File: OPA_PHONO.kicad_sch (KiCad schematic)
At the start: 5 parts, among them J1 PJRAS2X1S01X, J2 PJRAS2X1S01X, J3 UJC-HP-3-SMT-TR

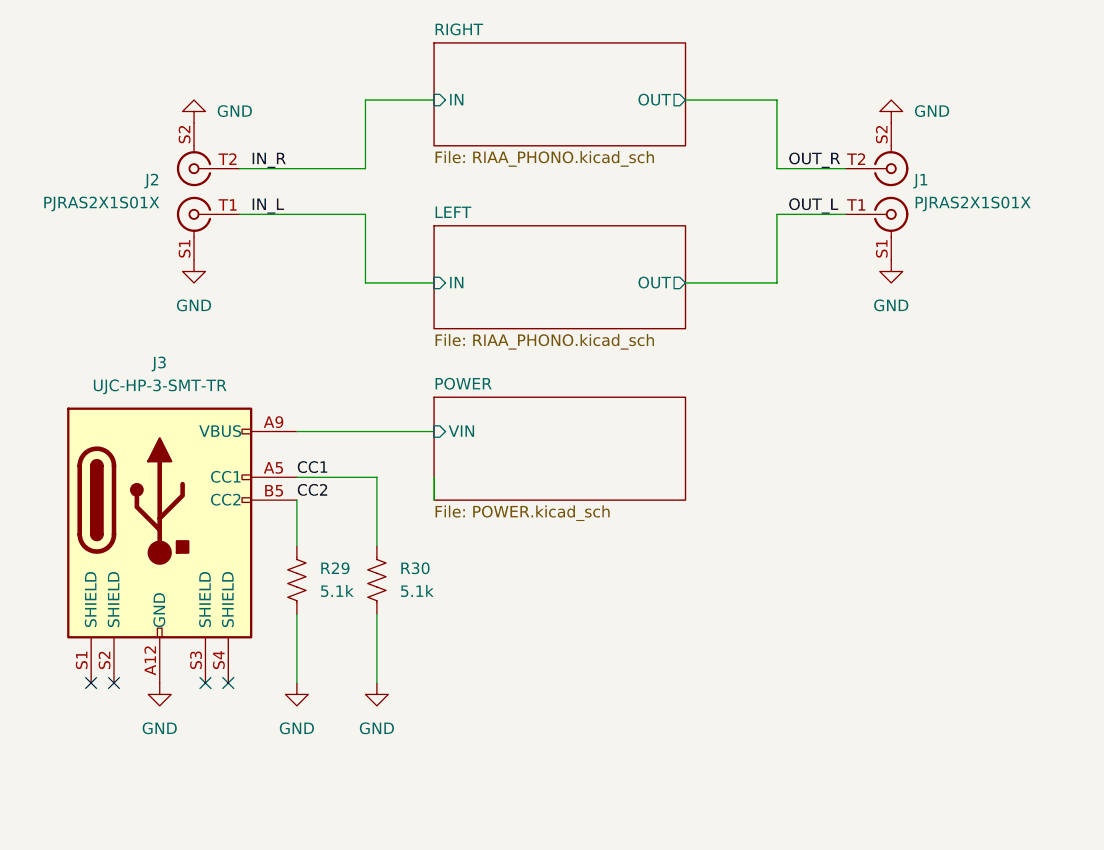
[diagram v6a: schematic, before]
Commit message: simplify BOM
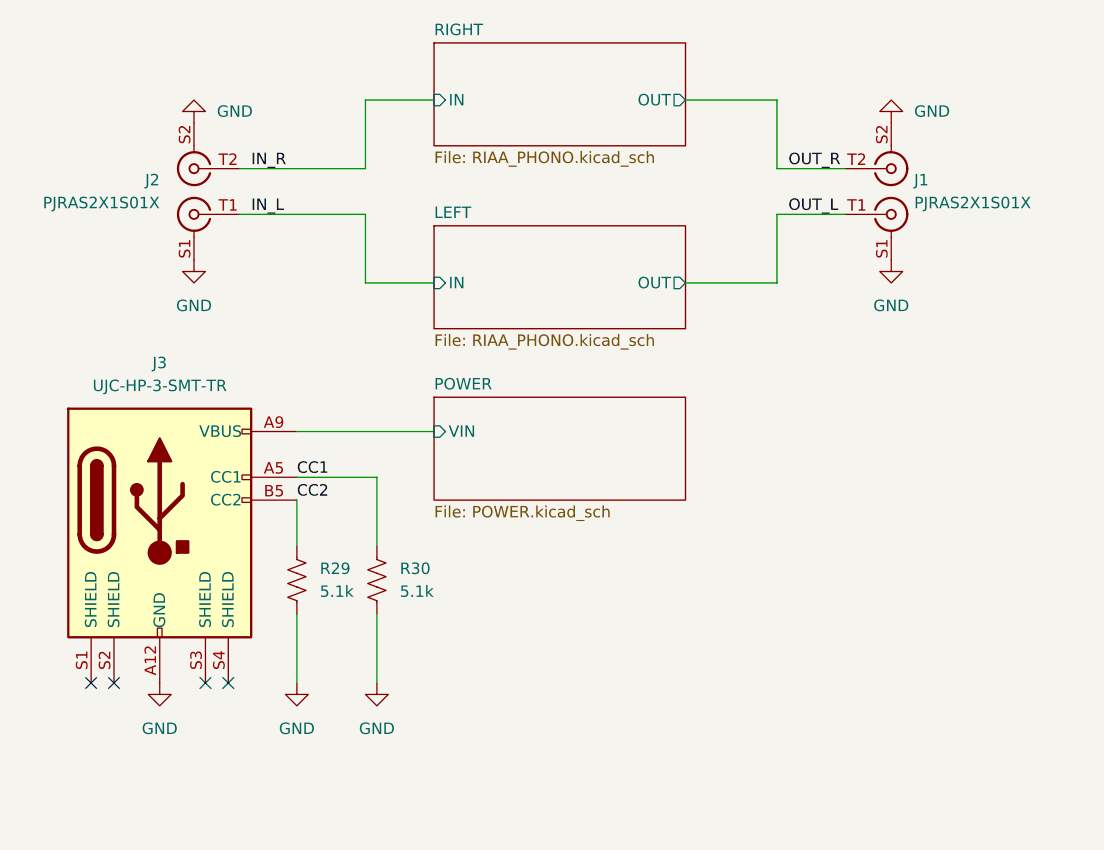
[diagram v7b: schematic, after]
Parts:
- R29, R30: Size (none) -> 0402; Tolerance (none) -> 1%
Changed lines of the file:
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@@
-    (stroke (width 0) (type default) (color 0 0 0 0))
-  )
-  (wire (pts (xy 158.75 104.14) (xy 158.75 106.68))
     (stroke (width 0) (type default) (color 0 0 0 0))
   )
@@
     )
     (property "Manufacturer" "YAGEO" (id 6) (at 152.4 115.57 0)
+      (effects (font (size 1.27 1.27)) hide)
+    )
+    (property "Size" "0402" (id 7) (at 152.4 115.57 0)
+      (effects (font (size 1.27 1.27)) hide)
+    )
+    (property "Tolerance" "1%" (id 8) (at 152.4 115.57 0)
       (effects (font (size 1.27 1.27)) hide)
     )
@@
       (effects (font (size 1.27 1.27)) hide)
     )
+    (property "Size" "0402" (id 7) (at 143.51 115.57 0)
+      (effects (font (size 1.27 1.27)) hide)
+    )
+    (property "Tolerance" "1%" (id 8) (at 143.51 115.57 0)
+      (effects (font (size 1.27 1.27)) hide)
+    )
     (pin "1")
     (pin "2")
@@
       (reference "#PWR01") (unit 1) (value "GND") (footprint "")
     )
-    (path "/54617677-cfc6-4c88-8682-59d8a487d34d/da9942e8-ea0f-4260-820c-4574caabdcb5"
-      (reference "#PWR02") (unit 1) (value "+12V") (footprint "")
-    )
     (path "/743e9973-c313-4d76-adf4-9efae6c3c3f1"
       (reference "#PWR03") (unit 1) (value "GND") (footprint "")
@@
       (reference "#PWR021") (unit 1) (value "GND") (footprint "")
     )
-    (path "/54617677-cfc6-4c88-8682-59d8a487d34d/2591e975-4607-4aea-9328-a52f454ef800"
-      (reference "#PWR022") (unit 1) (value "-12V") (footprint "")
-    )
     (path "/54617677-cfc6-4c88-8682-59d8a487d34d/fefc8354-6996-41d6-9839-a7fe6d0d8449"
       (reference "#PWR023") (unit 1) (value "GND") (footprint "")
@@
       (reference "#PWR025") (unit 1) (value "GND") (footprint "")
     )
-    (path "/54617677-cfc6-4c88-8682-59d8a487d34d/c269cfd8-5b8f-4de0-b20e-7c84acf71936"
-      (reference "#PWR026") (unit 1) (value "+12V") (footprint "")
-    )
-    (path "/54617677-cfc6-4c88-8682-59d8a487d34d/dd1e1934-bad6-4b43-8123-3dc71931d7c3"
-      (reference "#PWR027") (unit 1) (value "GND") (footprint "")
-    )
-    (path "/54617677-cfc6-4c88-8682-59d8a487d34d/3bb06c50-a15f-458d-bdd7-7b60a432303f"
-      (reference "#PWR028") (unit 1) (value "-12V") (footprint "")
-    )
     (path "/54617677-cfc6-4c88-8682-59d8a487d34d/68aca4e9-e183-4e64-a4df-ea2da42ffd61"
       (reference "#PWR029") (unit 1) (value "GND") (footprint "")
@@
     )
     (path "/b71452ae-e2ec-4238-9d16-71d9677f964c/1c569c2b-8416-4ca4-aafb-a8a73032326d"
-      (reference "R5") (unit 1) (value "2.2k") (footprint "Resistor_SMD:R_0402_1005Metric")
-    )
-    (path "/b71452ae-e2ec-4238-9d16-71d9677f964c/6dd6bcb6-0fe8-47b3-9062-5924fc5a0b35"
-      (reference "R6") (unit 1) (value "127R") (footprint "Resistor_SMD:R_0402_1005Metric")
+      (reference "R5") (unit 1) (value "2.32k") (footprint "Resistor_SMD:R_0402_1005Metric")
+    )
+    (path "/c67bced7-2ecb-4fda-afd4-a12d6372c9ce/c43a90e3-8027-448a-b17e-24673210d3e8"
+      (reference "R6") (unit 1) (value "100R") (footprint "Resistor_SMD:R_0402_1005Metric")
     )
     (path "/b71452ae-e2ec-4238-9d16-71d9677f964c/4abe7484-5a22-46f4-9ec2-8a46b020cb74"
       (reference "R7") (unit 1) (value "3.3k") (footprint "Resistor_SMD:R_0402_1005Metric")
     )
-    (path "/b71452ae-e2ec-4238-9d16-71d9677f964c/b1b0c55a-9762-46e5-8448-1bb4d9439fcf"
-      (reference "R8") (unit 1) (value "300R") (footprint "Resistor_SMD:R_0402_1005Metric")
+    (path "/b71452ae-e2ec-4238-9d16-71d9677f964c/c43a90e3-8027-448a-b17e-24673210d3e8"
+      (reference "R8") (unit 1) (value "100R") (footprint "Resistor_SMD:R_0402_1005Metric")
     )
     (path "/b71452ae-e2ec-4238-9d16-71d9677f964c/571ea169-b719-4431-95e4-90e0e9ab432b"
-      (reference "R9") (unit 1) (value "27.4k") (footprint "Resistor_SMD:R_0402_1005Metric")
+      (reference "R9") (unit 1) (value "47k") (footprint "Resistor_SMD:R_0402_1005Metric")
     )
     (path "/b71452ae-e2ec-4238-9d16-71d9677f964c/abcb5a34-06bc-4b19-8f6a-6f1b4a838911"
-      (reference "R10") (unit 1) (value "470k") (footprint "Resistor_SMD:R_0402_1005Metric")
+      (reference "R10") (unit 1) (value "47k") (footprint "Resistor_SMD:R_0402_1005Metric")
     )
     (path "/b71452ae-e2ec-4238-9d16-71d9677f964c/b3523fb5-67f3-4a1a-a0dc-6897a54d734e"
-      (reference "R11") (unit 1) (value "470k") (footprint "Resistor_SMD:R_0402_1005Metric")
+      (reference "R11") (unit 1) (value "47k") (footprint "Resistor_SMD:R_0402_1005Metric")
     )
     (path "/b71452ae-e2ec-4238-9d16-71d9677f964c/f4b75a43-3709-4216-bc55-c8fc3e9f3803"
@@
     )
     (path "/c67bced7-2ecb-4fda-afd4-a12d6372c9ce/1c569c2b-8416-4ca4-aafb-a8a73032326d"
-      (reference "R17") (unit 1) (value "2.2k") (footprint "Resistor_SMD:R_0402_1005Metric")
-    )
-    (path "/c67bced7-2ecb-4fda-afd4-a12d6372c9ce/6dd6bcb6-0fe8-47b3-9062-5924fc5a0b35"
-      (reference "R18") (unit 1) (value "127R") (footprint "Resistor_SMD:R_0402_1005Metric")
+      (reference "R17") (unit 1) (value "2.32k") (footprint "Resistor_SMD:R_0402_1005Metric")
     )
     (path "/c67bced7-2ecb-4fda-afd4-a12d6372c9ce/4abe7484-5a22-46f4-9ec2-8a46b020cb74"
       (reference "R19") (unit 1) (value "3.3k") (footprint "Resistor_SMD:R_0402_1005Metric")
     )
-    (path "/c67bced7-2ecb-4fda-afd4-a12d6372c9ce/b1b0c55a-9762-46e5-8448-1bb4d9439fcf"
-      (reference "R20") (unit 1) (value "300R") (footprint "Resistor_SMD:R_0402_1005Metric")
-    )
     (path "/c67bced7-2ecb-4fda-afd4-a12d6372c9ce/571ea169-b719-4431-95e4-90e0e9ab432b"
-      (reference "R21") (unit 1) (value "27.4k") (footprint "Resistor_SMD:R_0402_1005Metric")
+      (reference "R21") (unit 1) (value "47k") (footprint "Resistor_SMD:R_0402_1005Metric")
     )
     (path "/c67bced7-2ecb-4fda-afd4-a12d6372c9ce/abcb5a34-06bc-4b19-8f6a-6f1b4a838911"
-      (reference "R22") (unit 1) (value "470k") (footprint "Resistor_SMD:R_0402_1005Metric")
+      (reference "R22") (unit 1) (value "47k") (footprint "Resistor_SMD:R_0402_1005Metric")
     )
     (path "/c67bced7-2ecb-4fda-afd4-a12d6372c9ce/b3523fb5-67f3-4a1a-a0dc-6897a54d734e"
-      (reference "R23") (unit 1) (value "470k") (footprint "Resistor_SMD:R_0402_1005Metric")
+      (reference "R23") (unit 1) (value "47k") (footprint "Resistor_SMD:R_0402_1005Metric")
     )
     (path "/c67bced7-2ecb-4fda-afd4-a12d6372c9ce/f4b75a43-3709-4216-bc55-c8fc3e9f3803"
@@
     )
     (path "/54617677-cfc6-4c88-8682-59d8a487d34d/b04d0916-d162-498b-ac03-ae7e83849a3c"
-      (reference "R25") (unit 1) (value "470k") (footprint "Resistor_SMD:R_0402_1005Metric")
+      (reference "R25") (unit 1) (value "20.5k") (footprint "Resistor_SMD:R_0402_1005Metric")
     )
     (path "/54617677-cfc6-4c88-8682-59d8a487d34d/0b818ef6-6d67-45a8-a721-0eb2da9e535e"
-      (reference "R26") (unit 1) (value "120k") (footprint "Resistor_SMD:R_0402_1005Metric")
+      (reference "R26") (unit 1) (value "5.1k") (footprint "Resistor_SMD:R_0402_1005Metric")
     )
     (path "/54617677-cfc6-4c88-8682-59d8a487d34d/2370d309-51d1-439d-9ea5-e9e5954b7bfd"
-      (reference "R27") (unit 1) (value "120k") (footprint "Resistor_SMD:R_0402_1005Metric")
+      (reference "R27") (unit 1) (value "5.1k") (footprint "Resistor_SMD:R_0402_1005Metric")
     )
     (path "/54617677-cfc6-4c88-8682-59d8a487d34d/a7219ec4-c377-4c26-992e-ab18e8fa920b"
-      (reference "R28") (unit 1) (value "470k") (footprint "Resistor_SMD:R_0402_1005Metric")
+      (reference "R28") (unit 1) (value "20.5k") (footprint "Resistor_SMD:R_0402_1005Metric")
     )
     (path "/7afb76b2-51e4-4864-8977-34c565679c2b"
